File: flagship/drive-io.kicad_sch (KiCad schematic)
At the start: 11 parts, among them J4 DRIVE_COMMS, J5 DRIVE_MOTION, U10 74AHCT125, U9 THVD1450

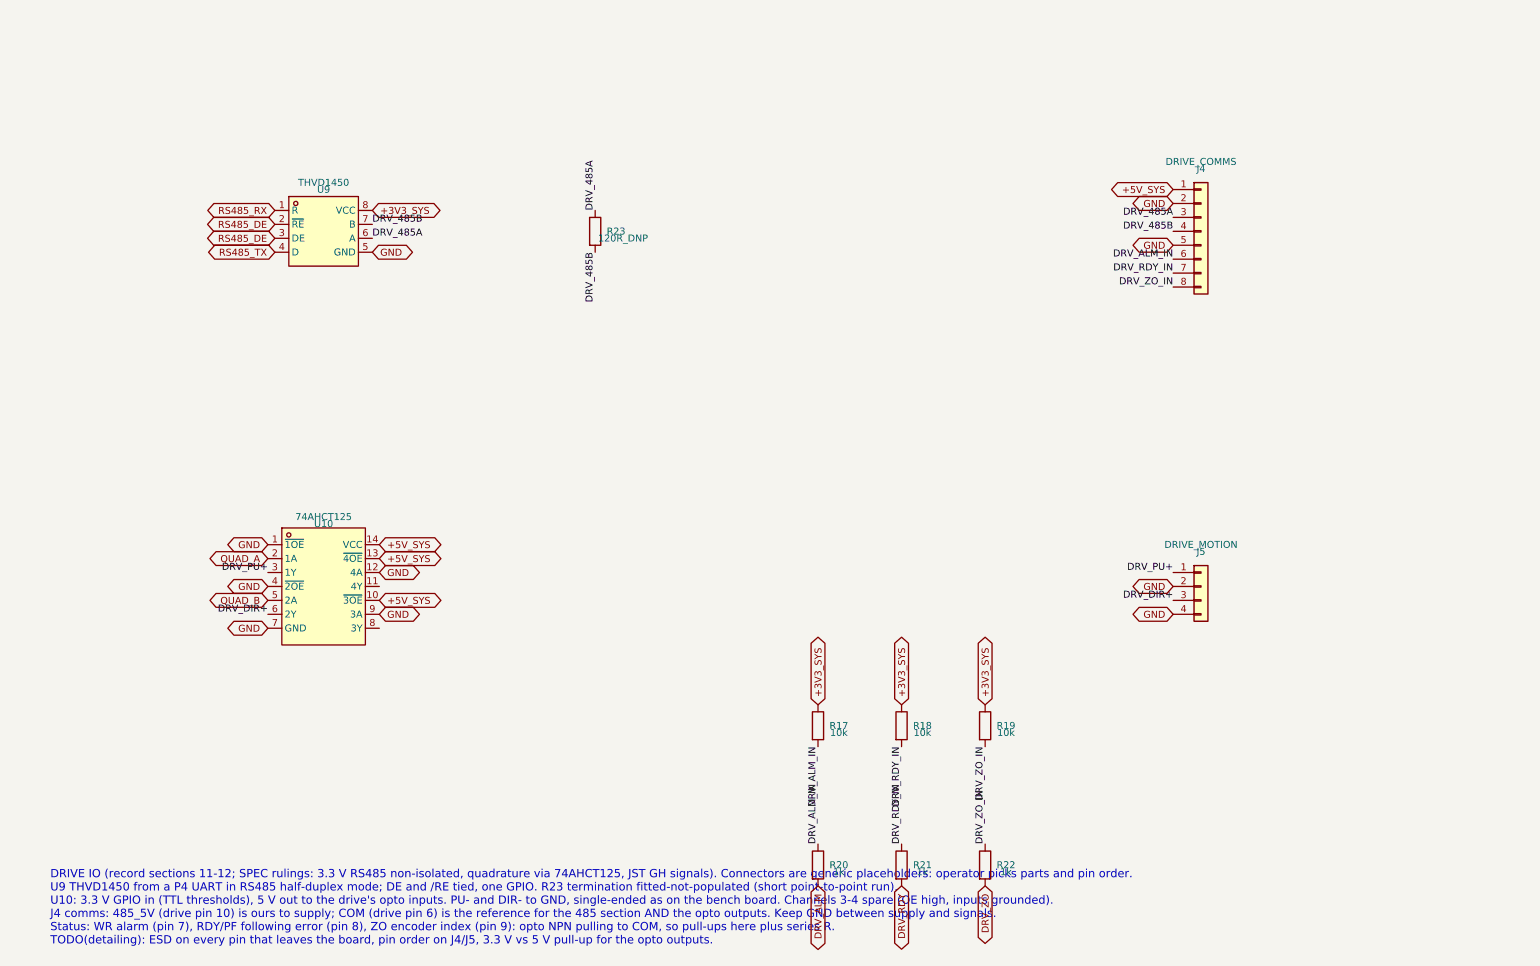
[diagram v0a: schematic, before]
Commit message: flagship: Drive IO detailed and drawn wired; connectors left to the operator (named nets)
RS485 (THVD1450, DE and /RE tied, 120 R DNP, SM712 ESD), quadrature buffers (KiCad
74AHCT125 per-gate symbol, spare gates disabled and no-connect), three status inputs
(10k pull-up, 1k series). J4/J5 placeholders removed: every off-board net ends in a
global label (DRV_485A/B, DRV_PU+/DIR+, DRV_*_IN, +5V_SYS for 485_5V). SM712 pulled
from LCSC (C12067). Verified: all sheet nets match the intended topology; ERC errors are
only the four P4-driven inputs awaiting layout pin assignment.

Co-Authored-By: Claude Opus 5.5 (1M context) <noreply@anthropic.com>
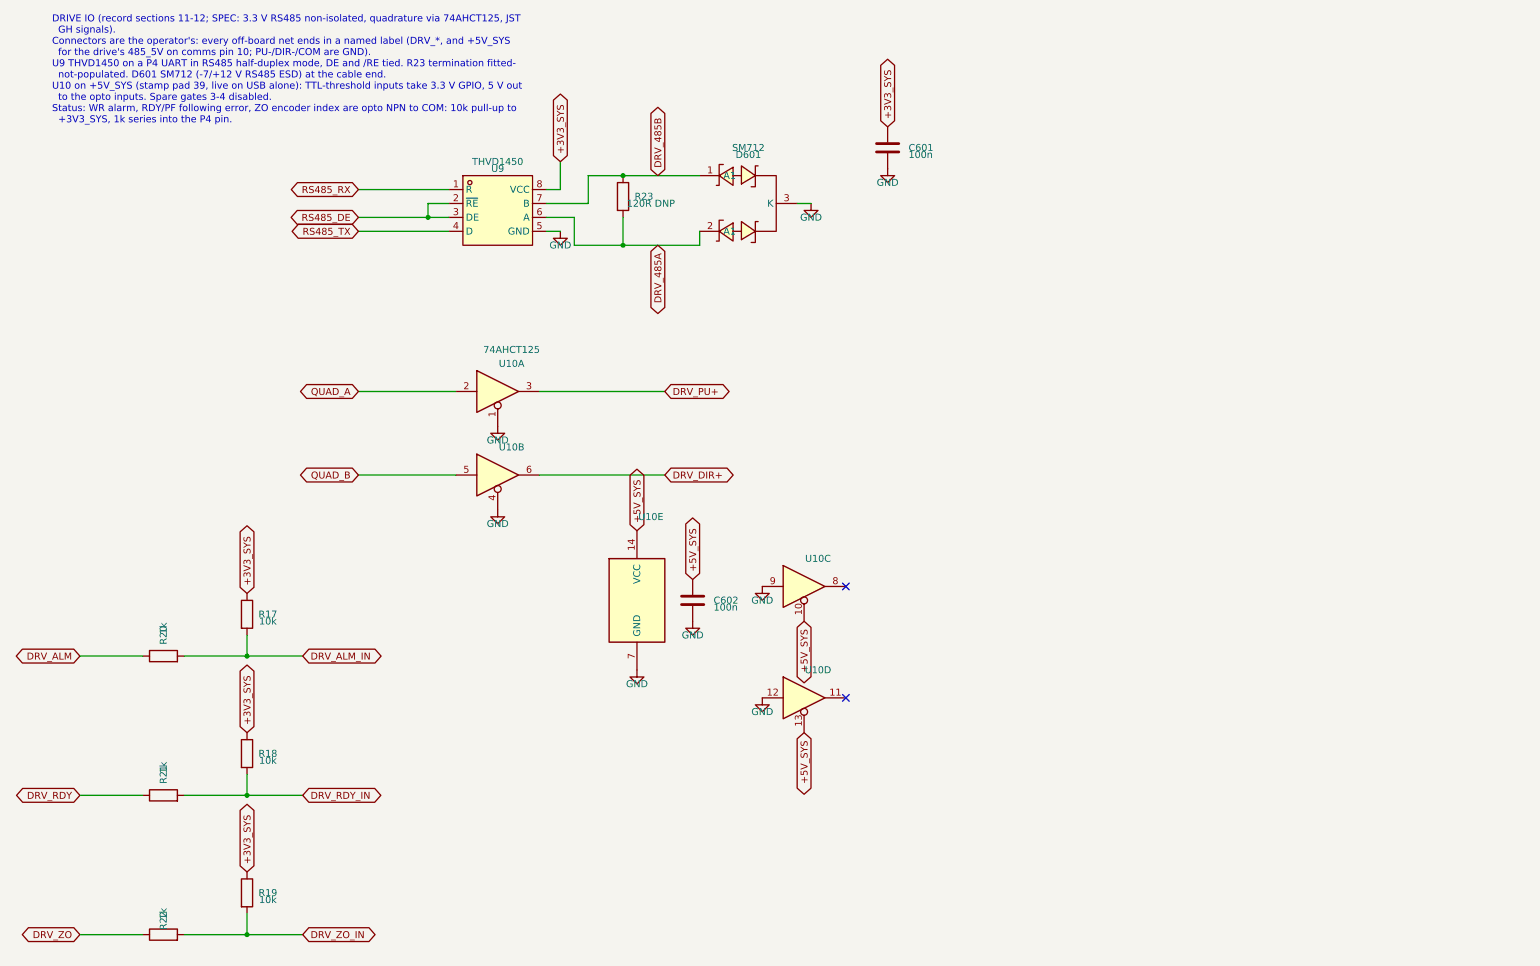
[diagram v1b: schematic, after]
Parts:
- removed J4: DRIVE_COMMS, symbol Connector_Generic:Conn_01x08
- removed J5: DRIVE_MOTION, symbol Connector_Generic:Conn_01x04
- removed U10: 74AHCT125, flagship:TSSOP-14_L5.0-W4.4-P0.65-LS6.4-BL, symbol flagship:SN74AHCT125PWR
- added C601, C602: 100n, Capacitor_SMD:C_0805_2012Metric, symbol Device:C
- added D601: SM712, flagship:SOT-23-3_L3.0-W1.7-P0.95-LS2.9-BR, symbol flagship:SM712.TCT
- added U10: 74AHCT125, Package_SO:TSSOP-14_4.4x5mm_P0.65mm, symbol 74xx:74AHCT125
- R23: value 120R_DNP -> 120R DNP
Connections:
- net +3V3_SYS: now also C601.1
- net +5V_SYS: now also C602.1, U10.10, U10.13, U10.14 (VCC)
- net DRV_485A: now also R23.2, D601.2 (A1); no longer R23.1
- net DRV_485B: now also R23.1, D601.1 (A1); no longer R23.2
- net DRV_ALM: now also R20.1; no longer R20.2
- net DRV_ALM_IN: now also R20.2; no longer R20.1
- net DRV_DIR+: now also U10.6
- net DRV_PU+: now also U10.3
- net DRV_RDY: now also R21.1; no longer R21.2
- net DRV_RDY_IN: now also R21.2; no longer R21.1
- net DRV_ZO: now also R22.1; no longer R22.2
- net DRV_ZO_IN: now also R22.2; no longer R22.1
- net GND: now also C601.2, C602.2, D601.3 (K), U10.1, U10.12, U10.4, U10.7 (GND), U10.9
- net QUAD_A: now also U10.2
- net QUAD_B: now also U10.5
- no-connect marks 0 -> 2
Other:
- note added: "DRIVE IO (record sections 11-12; SPEC: 3.3 V RS485 non-isolated, quadrature via 74AHCT125, JST GH signals). Connectors are the operator's: every off-board net ends in a named label (DRV_*, and +5V_SYS for the drive's 485_5V on comms pin 10; PU-/DIR-/COM are GND). U9 THVD1450 on a P4 UART in RS485 half-duplex mode, DE and /RE tied. R23 termination fitted- not-populated. D601 SM712 (-7/+12 V RS485 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"
- note removed: "DRIVE IO (record sections 11-12; SPEC rulings: 3.3 V RS485 non-isolated, quadrature via 74AHCT125, JST GH signals). Connectors are generic placeholders: operator picks parts and pin order. U9 THVD1450 from a P4 UART in RS485 half-duplex mode; DE and /RE tied, one GPIO. R23 termination fitted-not-populated (short point-to-point run). U10: 3.3 V GPIO in (TTL thresholds), 5 V out to the drive's opto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"
